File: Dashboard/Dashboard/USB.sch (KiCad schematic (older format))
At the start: 8 parts, among them J401 USB_B_Micro, U401 CP2102N-A01-GQFN24

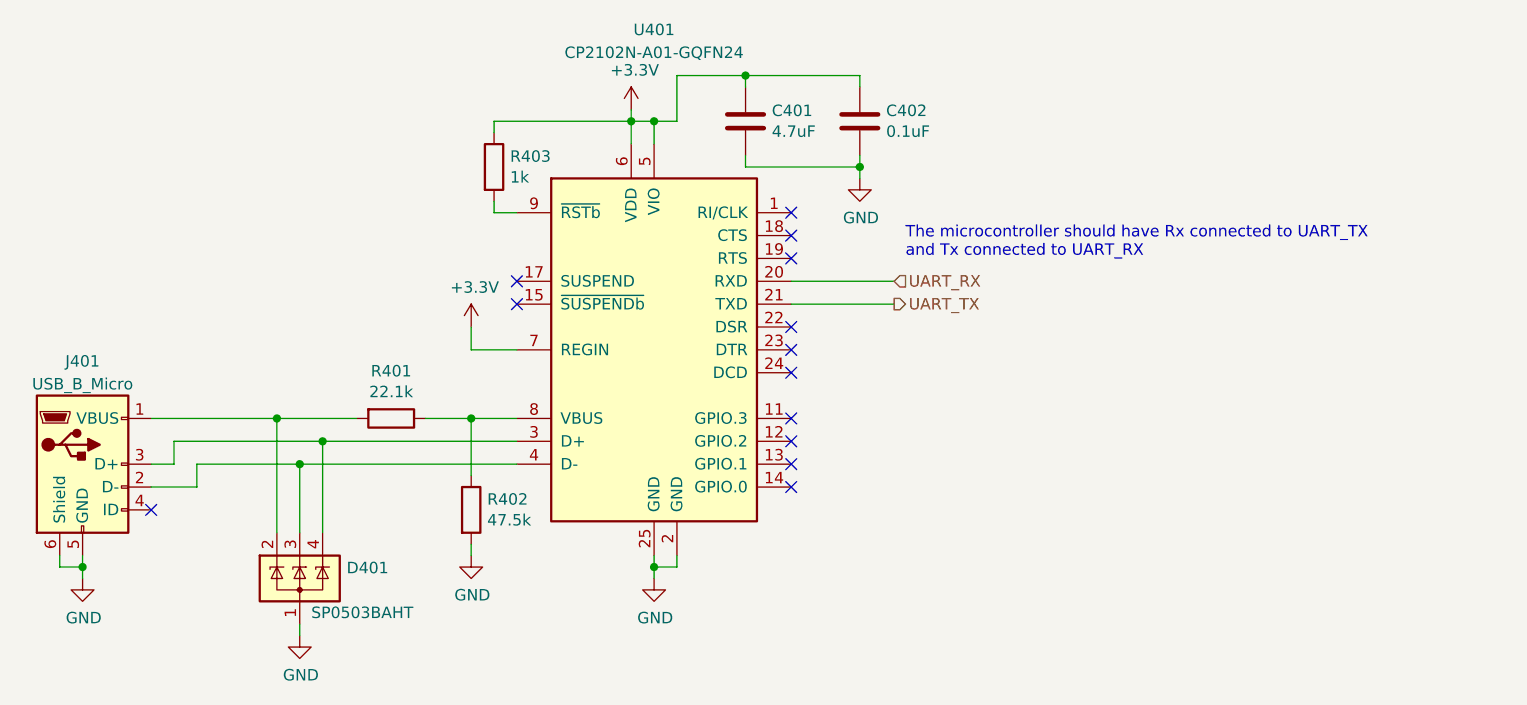
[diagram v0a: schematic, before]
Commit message: Change the MCU to the R (64-pin) variant.
Problem
=======
I don't want to have to solder 144 pins.

Solution
========
I changed the package of the MCU to the 64-pin
version, which now makes it the exact same as
the BPS.
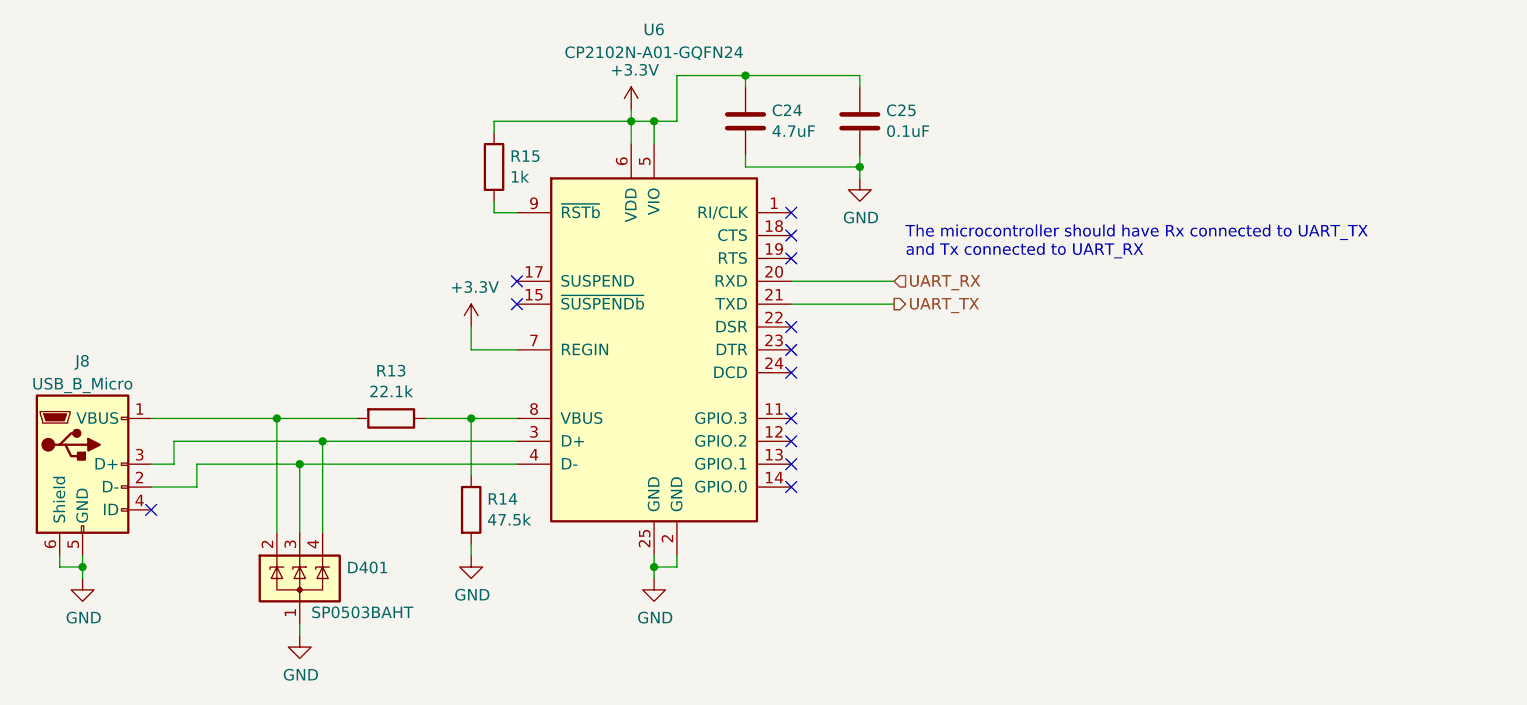
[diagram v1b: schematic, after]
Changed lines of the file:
@@
 U 1 1 5C4963B2
 P 5500 3800
-F 0 "U401" H 5500 5200 50  0000 C CNN
+AR Path="/5E91171A/5C4963B2" Ref="U401"  Part="1"
+AR Path="/5F7A9238/5C4963B2" Ref="U6"  Part="1"
+F 0 "U6" H 5500 5200 50  0000 C CNN
 F 1 "CP2102N-A01-GQFN24" H 5500 5100 50  0000 C CNN
 F 2 "Package_DFN_QFN:QFN-24-1EP_4x4mm_P0.5mm_EP2.6x2.6mm" H 5950 3000 50  0001 L CNN
@@
 U 1 1 5C4964BB
 P 3000 4300
-F 0 "J401" H 3000 4750 50  0000 C CNN
+AR Path="/5E91171A/5C4964BB" Ref="J401"  Part="1"
+AR Path="/5F7A9238/5C4964BB" Ref="J8"  Part="1"
+F 0 "J8" H 3000 4750 50  0000 C CNN
 F 1 "USB_B_Micro" H 3000 4650 50  0000 C CNN
 F 2 "Connector_USB:USB_Micro-B_Molex-105017-0001" H 3150 4250 50  0001 C CNN
@@
 U 1 1 5C4965DF
 P 3000 4800
-F 0 "#PWR0401" H 3000 4550 50  0001 C CNN
+AR Path="/5E91171A/5C4965DF" Ref="#PWR0401"  Part="1"
+AR Path="/5F7A9238/5C4965DF" Ref="#PWR0188"  Part="1"
+F 0 "#PWR0188" H 3000 4550 50  0001 C CNN
 F 1 "GND" H 3005 4627 50  0000 C CNN
 F 2 "" H 3000 4800 50  0001 C CNN
@@
 U 1 1 5C4966CF
 P 5500 4800
-F 0 "#PWR0406" H 5500 4550 50  0001 C CNN
+AR Path="/5E91171A/5C4966CF" Ref="#PWR0406"  Part="1"
+AR Path="/5F7A9238/5C4966CF" Ref="#PWR0189"  Part="1"
+F 0 "#PWR0189" H 5500 4550 50  0001 C CNN
 F 1 "GND" H 5505 4627 50  0000 C CNN
 F 2 "" H 5500 4800 50  0001 C CNN
@@
 U 1 1 5C496C9B
 P 3950 4800
-F 0 "D401" H 4155 4846 50  0000 L CNN
+AR Path="/5E91171A/5C496C9B" Ref="D401"  Part="1"
+AR Path="/5F7A9238/5C496C9B" Ref="D?"  Part="1"
+F 0 "D?" H 4155 4846 50  0000 L CNN
 F 1 "SP0503BAHT" H 4000 4650 50  0000 L CNN
 F 2 "Package_TO_SOT_SMD:SOT-143" H 4175 4750 50  0001 L CNN
@@
 U 1 1 5C497074
 P 3950 5050
-F 0 "#PWR0402" H 3950 4800 50  0001 C CNN
+AR Path="/5E91171A/5C497074" Ref="#PWR0402"  Part="1"
+AR Path="/5F7A9238/5C497074" Ref="#PWR0190"  Part="1"
+F 0 "#PWR0190" H 3950 4800 50  0001 C CNN
 F 1 "GND" H 3955 4877 50  0000 C CNN
 F 2 "" H 3950 5050 50  0001 C CNN
@@
 U 1 1 5C497DB9
 P 4700 4500
-F 0 "R402" H 4770 4546 50  0000 L CNN
+AR Path="/5E91171A/5C497DB9" Ref="R402"  Part="1"
+AR Path="/5F7A9238/5C497DB9" Ref="R14"  Part="1"
+F 0 "R14" H 4770 4546 50  0000 L CNN
 F 1 "47.5k" H 4770 4455 50  0000 L CNN
 F 2 "Resistor_SMD:R_0805_2012Metric" V 4630 4500 50  0001 C CNN
@@
 U 1 1 5C497DDB
 P 4350 4100
-F 0 "R401" V 4143 4100 50  0000 C CNN
+AR Path="/5E91171A/5C497DDB" Ref="R401"  Part="1"
+AR Path="/5F7A9238/5C497DDB" Ref="R13"  Part="1"
+F 0 "R13" V 4143 4100 50  0000 C CNN
 F 1 "22.1k" V 4234 4100 50  0000 C CNN
 F 2 "Resistor_SMD:R_0805_2012Metric" V 4280 4100 50  0001 C CNN
@@
 U 1 1 5C498DBE
 P 4700 4700
-F 0 "#PWR0404" H 4700 4450 50  0001 C CNN
+AR Path="/5E91171A/5C498DBE" Ref="#PWR0404"  Part="1"
+AR Path="/5F7A9238/5C498DBE" Ref="#PWR0191"  Part="1"
+F 0 "#PWR0191" H 4700 4450 50  0001 C CNN
 F 1 "GND" H 4705 4527 50  0000 C CNN
 F 2 "" H 4700 4700 50  0001 C CNN
@@
 U 1 1 5C499E7D
 P 5400 2750
-F 0 "#PWR0405" H 5400 2600 50  0001 C CNN
+AR Path="/5E91171A/5C499E7D" Ref="#PWR0405"  Part="1"
+AR Path="/5F7A9238/5C499E7D" Ref="#PWR0192"  Part="1"
+F 0 "#PWR0192" H 5400 2600 50  0001 C CNN
 F 1 "+3.3V" H 5415 2923 50  0000 C CNN
 F 2 "" H 5400 2750 50  0001 C CNN
@@
 U 1 1 5C49B01B
 P 4800 3000
-F 0 "R403" H 4870 3046 50  0000 L CNN
+AR Path="/5E91171A/5C49B01B" Ref="R403"  Part="1"
+AR Path="/5F7A9238/5C49B01B" Ref="R15"  Part="1"
+F 0 "R15" H 4870 3046 50  0000 L CNN
 F 1 "1k" H 4870 2955 50  0000 L CNN
 F 2 "Resistor_SMD:R_0805_2012Metric" V 4730 3000 50  0001 C CNN
@@
 U 1 1 5C49CC52
 P 5900 2800
-F 0 "C401" H 6015 2846 50  0000 L CNN
+AR Path="/5E91171A/5C49CC52" Ref="C401"  Part="1"
+AR Path="/5F7A9238/5C49CC52" Ref="C24"  Part="1"
+F 0 "C24" H 6015 2846 50  0000 L CNN
 F 1 "4.7uF" H 6015 2755 50  0000 L CNN
 F 2 "Capacitor_SMD:C_0805_2012Metric" H 5938 2650 50  0001 C CNN
@@
 U 1 1 5C4A2CBF
 P 4700 3700
-F 0 "#PWR0403" H 4700 3550 50  0001 C CNN
+AR Path="/5E91171A/5C4A2CBF" Ref="#PWR0403"  Part="1"
+AR Path="/5F7A9238/5C4A2CBF" Ref="#PWR0193"  Part="1"
+F 0 "#PWR0193" H 4700 3550 50  0001 C CNN
 F 1 "+3.3V" H 4715 3873 50  0000 C CNN
 F 2 "" H 4700 3700 50  0001 C CNN
@@
 U 1 1 5C4A4791
 P 6400 2800
-F 0 "C402" H 6515 2846 50  0000 L CNN
+AR Path="/5E91171A/5C4A4791" Ref="C402"  Part="1"
+AR Path="/5F7A9238/5C4A4791" Ref="C25"  Part="1"
+F 0 "C25" H 6515 2846 50  0000 L CNN
 F 1 "0.1uF" H 6515 2755 50  0000 L CNN
 F 2 "Capacitor_SMD:C_0805_2012Metric" H 6438 2650 50  0001 C CNN
@@
 U 1 1 5C4A4BE4
 P 6400 3050
-F 0 "#PWR0407" H 6400 2800 50  0001 C CNN
+AR Path="/5E91171A/5C4A4BE4" Ref="#PWR0407"  Part="1"
+AR Path="/5F7A9238/5C4A4BE4" Ref="#PWR0194"  Part="1"
+F 0 "#PWR0194" H 6400 2800 50  0001 C CNN
 F 1 "GND" H 6405 2877 50  0000 C CNN
 F 2 "" H 6400 3050 50  0001 C CNN

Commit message: Add redundant potentiometers and relabel components.
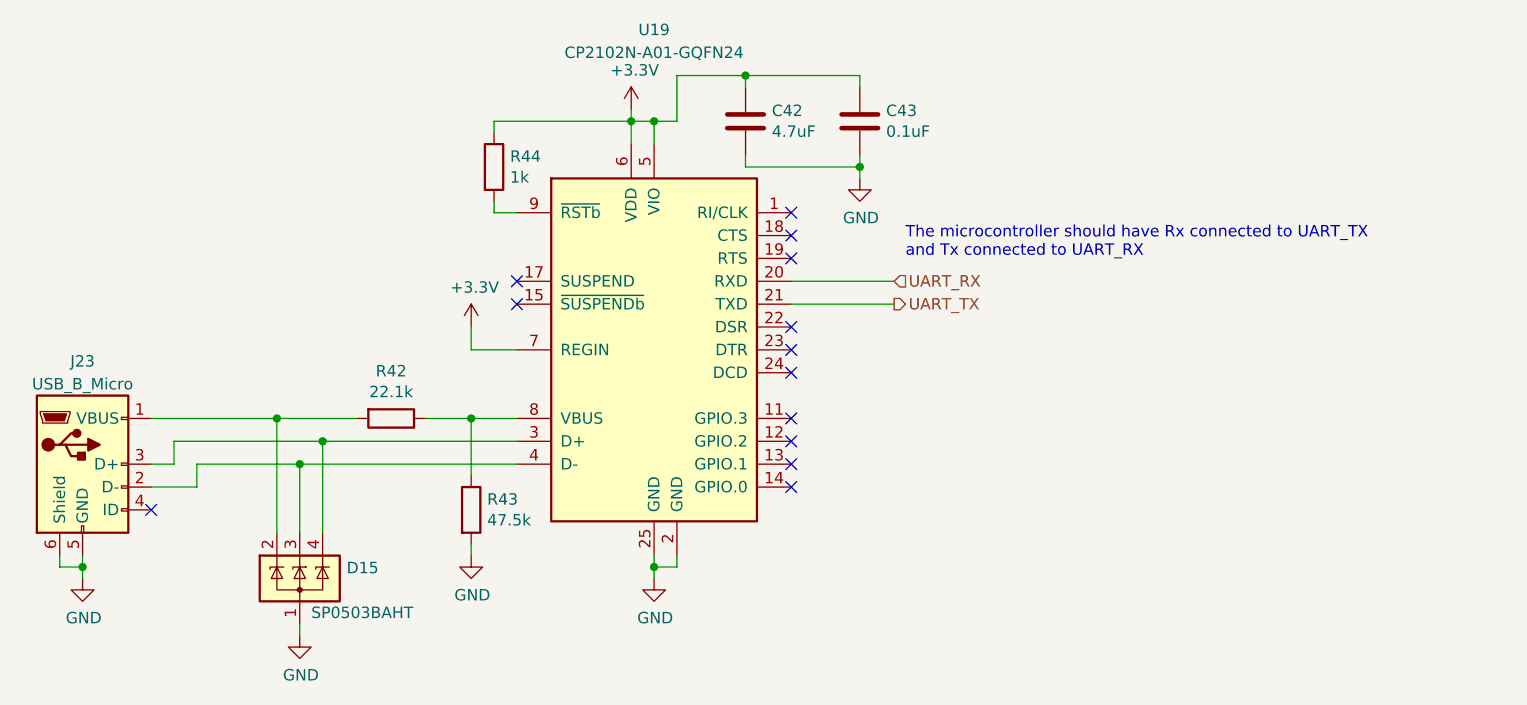
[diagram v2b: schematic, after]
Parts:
- renumbered C401 to C42, C402 to C43, D401 to D15, J401 to J23, R401 to R42, R402 to R43, R403 to R44, U401 to U19
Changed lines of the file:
@@
 $Descr A4 11693 8268
 encoding utf-8
-Sheet 4 6
+Sheet 6 6
 Title ""
 Date ""
@@
 $EndDescr
 $Comp
-L Interface_USB:CP2102N-A01-GQFN24 U401
+L Interface_USB:CP2102N-A01-GQFN24 U?
 U 1 1 5C4963B2
 P 5500 3800
-AR Path="/5E91171A/5C4963B2" Ref="U401"  Part="1"
-AR Path="/5F7A9238/5C4963B2" Ref="U6"  Part="1"
-F 0 "U6" H 5500 5200 50  0000 C CNN
+AR Path="/5E91171A/5C4963B2" Ref="U?"  Part="1"
+AR Path="/5F7A9238/5C4963B2" Ref="U19"  Part="1"
+F 0 "U19" H 5500 5200 50  0000 C CNN
 F 1 "CP2102N-A01-GQFN24" H 5500 5100 50  0000 C CNN
 F 2 "Package_DFN_QFN:QFN-24-1EP_4x4mm_P0.5mm_EP2.6x2.6mm" H 5950 3000 50  0001 L CNN
@@
 $EndComp
 $Comp
-L Connector:USB_B_Micro J401
+L Connector:USB_B_Micro J?
 U 1 1 5C4964BB
 P 3000 4300
-AR Path="/5E91171A/5C4964BB" Ref="J401"  Part="1"
-AR Path="/5F7A9238/5C4964BB" Ref="J8"  Part="1"
-F 0 "J8" H 3000 4750 50  0000 C CNN
+AR Path="/5E91171A/5C4964BB" Ref="J?"  Part="1"
+AR Path="/5F7A9238/5C4964BB" Ref="J23"  Part="1"
+F 0 "J23" H 3000 4750 50  0000 C CNN
 F 1 "USB_B_Micro" H 3000 4650 50  0000 C CNN
 F 2 "Connector_USB:USB_Micro-B_Molex-105017-0001" H 3150 4250 50  0001 C CNN
@@
 	3500 4400 3500 4300
 $Comp
-L power:GND #PWR0401
+L power:GND #PWR?
 U 1 1 5C4965DF
 P 3000 4800
-AR Path="/5E91171A/5C4965DF" Ref="#PWR0401"  Part="1"
-AR Path="/5F7A9238/5C4965DF" Ref="#PWR0188"  Part="1"
-F 0 "#PWR0188" H 3000 4550 50  0001 C CNN
+AR Path="/5E91171A/5C4965DF" Ref="#PWR?"  Part="1"
+AR Path="/5F7A9238/5C4965DF" Ref="#PWR0101"  Part="1"
+F 0 "#PWR0101" H 3000 4550 50  0001 C CNN
 F 1 "GND" H 3005 4627 50  0000 C CNN
 F 2 "" H 3000 4800 50  0001 C CNN
@@
 Connection ~ 3000 4750
 $Comp
-L power:GND #PWR0406
+L power:GND #PWR?
 U 1 1 5C4966CF
 P 5500 4800
-AR Path="/5E91171A/5C4966CF" Ref="#PWR0406"  Part="1"
-AR Path="/5F7A9238/5C4966CF" Ref="#PWR0189"  Part="1"
-F 0 "#PWR0189" H 5500 4550 50  0001 C CNN
+AR Path="/5E91171A/5C4966CF" Ref="#PWR?"  Part="1"
+AR Path="/5F7A9238/5C4966CF" Ref="#PWR0106"  Part="1"
+F 0 "#PWR0106" H 5500 4550 50  0001 C CNN
 F 1 "GND" H 5505 4627 50  0000 C CNN
 F 2 "" H 5500 4800 50  0001 C CNN
@@
 	5500 4750 5500 4800
 $Comp
-L Dash2-rescue:SP0503BAHT-Power_Protection D401
+L Dash2-rescue:SP0503BAHT-Power_Protection D?
 U 1 1 5C496C9B
 P 3950 4800
-AR Path="/5E91171A/5C496C9B" Ref="D401"  Part="1"
-AR Path="/5F7A9238/5C496C9B" Ref="D?"  Part="1"
-F 0 "D?" H 4155 4846 50  0000 L CNN
+AR Path="/5E91171A/5C496C9B" Ref="D?"  Part="1"
+AR Path="/5F7A9238/5C496C9B" Ref="D15"  Part="1"
+F 0 "D15" H 4155 4846 50  0000 L CNN
 F 1 "SP0503BAHT" H 4000 4650 50  0000 L CNN
 F 2 "Package_TO_SOT_SMD:SOT-143" H 4175 4750 50  0001 L CNN
@@
 $EndComp
 $Comp
-L power:GND #PWR0402
+L power:GND #PWR?
 U 1 1 5C497074
 P 3950 5050
-AR Path="/5E91171A/5C497074" Ref="#PWR0402"  Part="1"
-AR Path="/5F7A9238/5C497074" Ref="#PWR0190"  Part="1"
-F 0 "#PWR0190" H 3950 4800 50  0001 C CNN
+AR Path="/5E91171A/5C497074" Ref="#PWR?"  Part="1"
+AR Path="/5F7A9238/5C497074" Ref="#PWR0102"  Part="1"
+F 0 "#PWR0102" H 3950 4800 50  0001 C CNN
 F 1 "GND" H 3955 4877 50  0000 C CNN
 F 2 "" H 3950 5050 50  0001 C CNN
@@
 	3850 4600 3850 4100
 $Comp
-L Device:R R402
+L Device:R R?
 U 1 1 5C497DB9
 P 4700 4500
-AR Path="/5E91171A/5C497DB9" Ref="R402"  Part="1"
-AR Path="/5F7A9238/5C497DB9" Ref="R14"  Part="1"
-F 0 "R14" H 4770 4546 50  0000 L CNN
+AR Path="/5E91171A/5C497DB9" Ref="R?"  Part="1"
+AR Path="/5F7A9238/5C497DB9" Ref="R43"  Part="1"
+F 0 "R43" H 4770 4546 50  0000 L CNN
 F 1 "47.5k" H 4770 4455 50  0000 L CNN
 F 2 "Resistor_SMD:R_0805_2012Metric" V 4630 4500 50  0001 C CNN
@@
 $EndComp
 $Comp
-L Device:R R401
+L Device:R R?
 U 1 1 5C497DDB
 P 4350 4100
-AR Path="/5E91171A/5C497DDB" Ref="R401"  Part="1"
-AR Path="/5F7A9238/5C497DDB" Ref="R13"  Part="1"
-F 0 "R13" V 4143 4100 50  0000 C CNN
+AR Path="/5E91171A/5C497DDB" Ref="R?"  Part="1"
+AR Path="/5F7A9238/5C497DDB" Ref="R42"  Part="1"
+F 0 "R42" V 4143 4100 50  0000 C CNN
 F 1 "22.1k" V 4234 4100 50  0000 C CNN
 F 2 "Resistor_SMD:R_0805_2012Metric" V 4280 4100 50  0001 C CNN
@@
 	4200 4100 3850 4100
 $Comp
-L power:GND #PWR0404
+L power:GND #PWR?
 U 1 1 5C498DBE
 P 4700 4700
-AR Path="/5E91171A/5C498DBE" Ref="#PWR0404"  Part="1"
-AR Path="/5F7A9238/5C498DBE" Ref="#PWR0191"  Part="1"
-F 0 "#PWR0191" H 4700 4450 50  0001 C CNN
+AR Path="/5E91171A/5C498DBE" Ref="#PWR?"  Part="1"
+AR Path="/5F7A9238/5C498DBE" Ref="#PWR0104"  Part="1"
+F 0 "#PWR0104" H 4700 4450 50  0001 C CNN
 F 1 "GND" H 4705 4527 50  0000 C CNN
 F 2 "" H 4700 4700 50  0001 C CNN
@@
 	4700 4700 4700 4650
 $Comp
-L power:+3.3V #PWR0405
+L power:+3.3V #PWR?
 U 1 1 5C499E7D
 P 5400 2750
-AR Path="/5E91171A/5C499E7D" Ref="#PWR0405"  Part="1"
-AR Path="/5F7A9238/5C499E7D" Ref="#PWR0192"  Part="1"
-F 0 "#PWR0192" H 5400 2600 50  0001 C CNN
+AR Path="/5E91171A/5C499E7D" Ref="#PWR?"  Part="1"
+AR Path="/5F7A9238/5C499E7D" Ref="#PWR0105"  Part="1"
+F 0 "#PWR0105" H 5400 2600 50  0001 C CNN
 F 1 "+3.3V" H 5415 2923 50  0000 C CNN
 F 2 "" H 5400 2750 50  0001 C CNN
@@
 Connection ~ 5400 2800
 $Comp
-L Device:R R403
+L Device:R R?
 U 1 1 5C49B01B
 P 4800 3000
-AR Path="/5E91171A/5C49B01B" Ref="R403"  Part="1"
-AR Path="/5F7A9238/5C49B01B" Ref="R15"  Part="1"
-F 0 "R15" H 4870 3046 50  0000 L CNN
+AR Path="/5E91171A/5C49B01B" Ref="R?"  Part="1"
+AR Path="/5F7A9238/5C49B01B" Ref="R44"  Part="1"
+F 0 "R44" H 4870 3046 50  0000 L CNN
 F 1 "1k" H 4870 2955 50  0000 L CNN
 F 2 "Resistor_SMD:R_0805_2012Metric" V 4730 3000 50  0001 C CNN
@@
 	4800 2800 5400 2800
 $Comp
-L Device:C C401
+L Device:C C?
 U 1 1 5C49CC52
 P 5900 2800
-AR Path="/5E91171A/5C49CC52" Ref="C401"  Part="1"
-AR Path="/5F7A9238/5C49CC52" Ref="C24"  Part="1"
-F 0 "C24" H 6015 2846 50  0000 L CNN
+AR Path="/5E91171A/5C49CC52" Ref="C?"  Part="1"
+AR Path="/5F7A9238/5C49CC52" Ref="C42"  Part="1"
+F 0 "C42" H 6015 2846 50  0000 L CNN
 F 1 "4.7uF" H 6015 2755 50  0000 L CNN
 F 2 "Capacitor_SMD:C_0805_2012Metric" H 5938 2650 50  0001 C CNN
@@
 NoConn ~ 6100 4400
 $Comp
-L power:+3.3V #PWR0403
+L power:+3.3V #PWR?
 U 1 1 5C4A2CBF
 P 4700 3700
-AR Path="/5E91171A/5C4A2CBF" Ref="#PWR0403"  Part="1"
-AR Path="/5F7A9238/5C4A2CBF" Ref="#PWR0193"  Part="1"
-F 0 "#PWR0193" H 4700 3550 50  0001 C CNN
+AR Path="/5E91171A/5C4A2CBF" Ref="#PWR?"  Part="1"
+AR Path="/5F7A9238/5C4A2CBF" Ref="#PWR0103"  Part="1"
+F 0 "#PWR0103" H 4700 3550 50  0001 C CNN
 F 1 "+3.3V" H 4715 3873 50  0000 C CNN
 F 2 "" H 4700 3700 50  0001 C CNN
@@
 	4700 3800 4900 3800
 $Comp
-L Device:C C402
+L Device:C C?
 U 1 1 5C4A4791
 P 6400 2800
-AR Path="/5E91171A/5C4A4791" Ref="C402"  Part="1"
-AR Path="/5F7A9238/5C4A4791" Ref="C25"  Part="1"
-F 0 "C25" H 6515 2846 50  0000 L CNN
+AR Path="/5E91171A/5C4A4791" Ref="C?"  Part="1"
+AR Path="/5F7A9238/5C4A4791" Ref="C43"  Part="1"
+F 0 "C43" H 6515 2846 50  0000 L CNN
 F 1 "0.1uF" H 6515 2755 50  0000 L CNN
 F 2 "Capacitor_SMD:C_0805_2012Metric" H 6438 2650 50  0001 C CNN
@@
 $EndComp
 $Comp
-L power:GND #PWR0407
+L power:GND #PWR?
 U 1 1 5C4A4BE4
 P 6400 3050
-AR Path="/5E91171A/5C4A4BE4" Ref="#PWR0407"  Part="1"
-AR Path="/5F7A9238/5C4A4BE4" Ref="#PWR0194"  Part="1"
-F 0 "#PWR0194" H 6400 2800 50  0001 C CNN
+AR Path="/5E91171A/5C4A4BE4" Ref="#PWR?"  Part="1"
+AR Path="/5F7A9238/5C4A4BE4" Ref="#PWR0107"  Part="1"
+F 0 "#PWR0107" H 6400 2800 50  0001 C CNN
 F 1 "GND" H 6405 2877 50  0000 C CNN
 F 2 "" H 6400 3050 50  0001 C CNN
